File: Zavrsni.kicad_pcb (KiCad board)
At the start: 2 copper layers, 139.7 x 81.3 mm, 7 parts, among them J1 JOYSTICK, J2 LSM6DS3, J3 ILI9341, J4 NUCLEO-H743ZI2, J5 NUCLEO-H743ZI2, J6 NUCLEO-H743ZI2, J7 NUCLEO-H743ZI2

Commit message: Add files via upload
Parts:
- added C1: 100 nF, Capacitor_SMD:C_0603_1608Metric, F.Cu at (47.9, 36.7)
- added C2: C, Capacitor_SMD:C_0603_1608Metric, F.Cu at (47.9, 39.2)
- added C3: C, Capacitor_SMD:C_0603_1608Metric, F.Cu at (47.9, 41.7)
- added C4: C, Capacitor_SMD:C_0603_1608Metric, F.Cu at (47.9, 44.2)
- added C5: C, Capacitor_SMD:C_0603_1608Metric, F.Cu at (47.9, 46.8)
- added R1: 10k, Resistor_SMD:R_0201_0603Metric, F.Cu at (51.1, 36.3)
- added R2: 10k, Resistor_SMD:R_0201_0603Metric, F.Cu at (51.1, 38.1)
- added R3: 10k, Resistor_SMD:R_0201_0603Metric, F.Cu at (51.1, 39.8)
- added R4: 10k, Resistor_SMD:R_0201_0603Metric, F.Cu at (51.1, 41.6)
- added R5: 10k, Resistor_SMD:R_0201_0603Metric, F.Cu at (51.1, 43.3)
- added R6: 10k, Resistor_SMD:R_0201_0603Metric, F.Cu at (51.1, 45.1)
- moved J7 90.0 mm to (106.0, 107.3)
- moved J5 19.0 mm to (154.3, 102.6), turned to 0 degrees
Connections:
- J3 pad 3: /CS -> Net-(J3-Pin_3)
- J3 pad 6: /SDI -> Net-(J3-Pin_6)
- J3 pad 7: /SCK -> Net-(J3-Pin_7)
- J3 pad 9: /SDO(MISO) -> Net-(J3-Pin_9)
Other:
- board size 139.7 x 81.3 mm -> 70 x 135 mm

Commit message: Add files via upload
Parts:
- added C6: 10nF, Capacitor_SMD:C_0603_1608Metric, F.Cu at (63.9, 108.3)
- added C7: 4,7uF, Capacitor_SMD:C_0603_1608Metric, F.Cu at (63.9, 110.8)
- added C8: 4,7uF, Capacitor_SMD:C_0603_1608Metric, F.Cu at (63.9, 113.3)
- added J8: Conn_02x35_Odd_Even, Connector_PinHeader_2.54mm:PinHeader_2x35_P2.54mm_Vertical, F.Cu at (248.3, 56.5)
- added J9: Conn_02x35_Odd_Even, Connector_PinHeader_2.54mm:PinHeader_2x35_P2.54mm_Vertical, F.Cu at (193.8, 56.5)
- added K1: JST-2pin-SMD, JST conector:jst connector, F.Cu at (63.6, 83.6)
- added R7: 10k, Resistor_SMD:R_0603_1608Metric, F.Cu at (63.9, 115.8)
- added SW1: SW_Push, Button_Switch_SMD:SW_Push_1P1T_NO_6x6mm_H9.5mm, F.Cu at (56.4, 110.8)
- added SW2: SW_Push, Button_Switch_SMD:SW_Push_1P1T_NO_6x6mm_H9.5mm, F.Cu at (56.4, 118.4)
- C2, C3, C4, C5: value C -> 100nF
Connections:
- net GND renamed Earth
- J5 pad 1: unconnected-(J5-Pin_1-Pad1) -> /D7
- J5 pad 4: unconnected-(J5-Pin_4-Pad4) -> /D4
- R5 pad 2: unconnected-(R5-Pad2) -> /D7
- R6 pad 1: unconnected-(R6-Pad1) -> +3.3V
- R6 pad 2: unconnected-(R6-Pad2) -> /D4
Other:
- board size 70 x 135 mm -> 151.2 x 133.3 mm

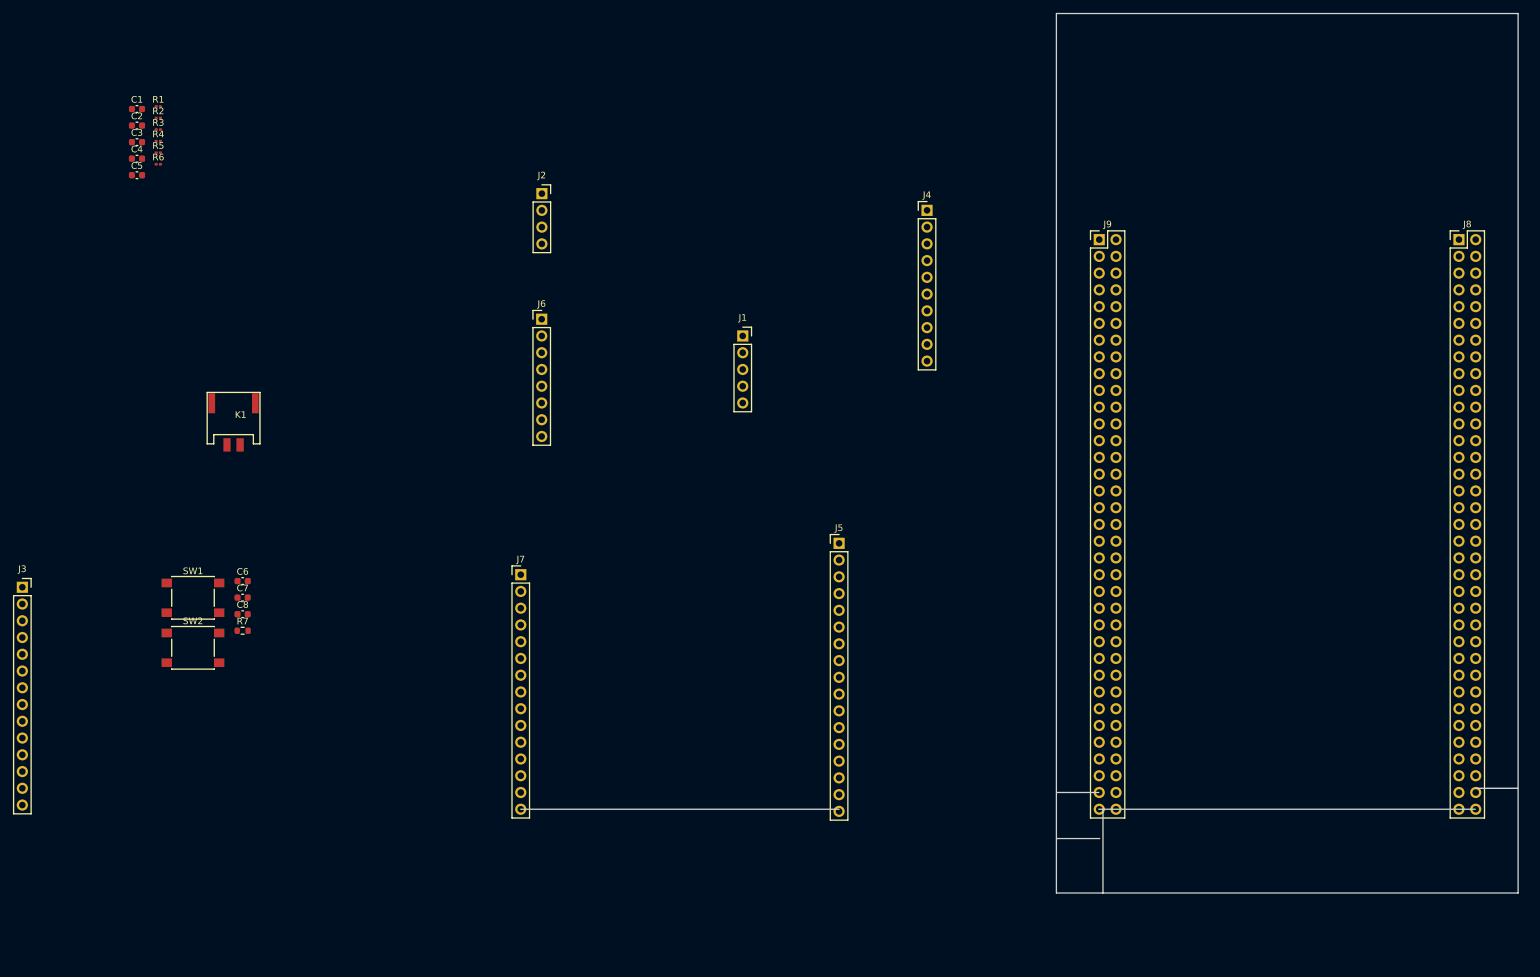
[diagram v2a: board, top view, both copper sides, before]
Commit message: Start connecting the lines on the pcb
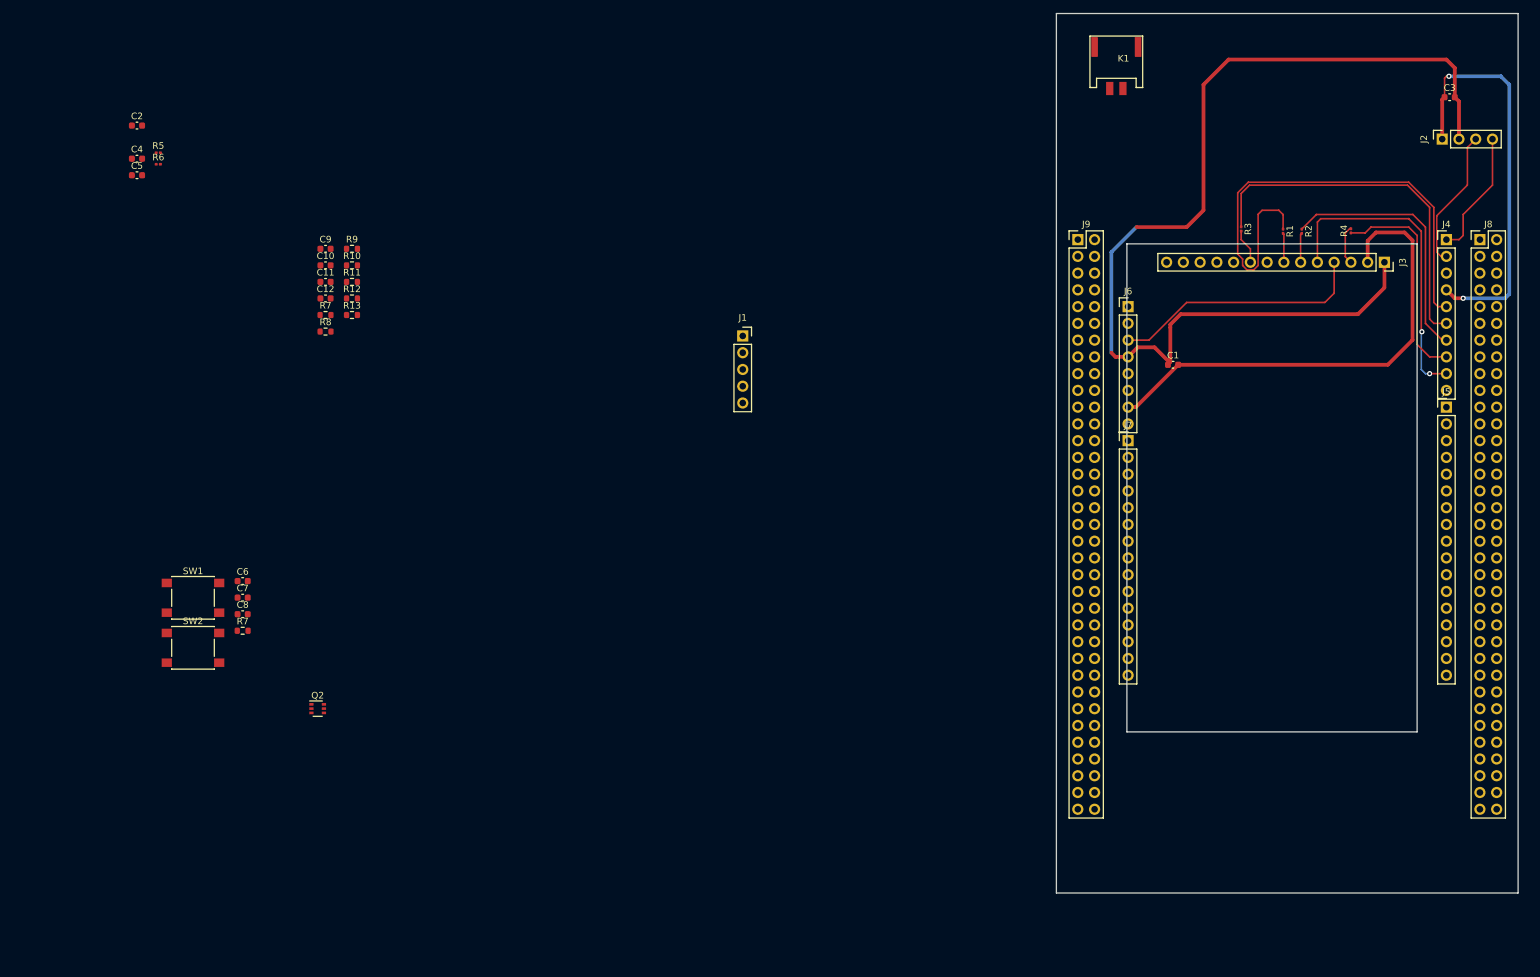
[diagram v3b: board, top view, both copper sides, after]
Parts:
- added C10: 10nF, Capacitor_SMD:C_0603_1608Metric, F.Cu at (76.4, 60.4)
- added C11: 10nF, Capacitor_SMD:C_0603_1608Metric, F.Cu at (76.4, 62.9)
- added C12: 10uF, Capacitor_SMD:C_0603_1608Metric, F.Cu at (76.4, 65.4)
- added C9: 10nF, Capacitor_SMD:C_0603_1608Metric, F.Cu at (76.4, 57.9)
- added Q2: BSD235C, Package_TO_SOT_SMD:SOT-363_SC-70-6, F.Cu at (75.2, 127.6)
- added R10: 100R, Resistor_SMD:R_0603_1608Metric, F.Cu at (80.5, 60.4)
- added R11: 10k, Resistor_SMD:R_0603_1608Metric, F.Cu at (80.5, 62.9)
- added R12: 100R, Resistor_SMD:R_0603_1608Metric, F.Cu at (80.5, 65.4)
- added R13: 100R, Resistor_SMD:R_0603_1608Metric, F.Cu at (80.5, 67.9)
- added R7: 1k, Resistor_SMD:R_0603_1608Metric, F.Cu at (76.4, 67.9)
- added R8: 100R, Resistor_SMD:R_0603_1608Metric, F.Cu at (76.4, 70.5)
- added R9: 100R, Resistor_SMD:R_0603_1608Metric, F.Cu at (80.5, 57.9)
- C6: value 10nF -> 10uF
- C7, C8: value 4,7uF -> 10nF
- R1, R2, R3, R4: value 10k -> 330R
- moved J3 212.3 mm to (237.0, 59.9), turned to -90 degrees
- moved C3 199.1 mm to (246.9, 34.9)
- moved R4 181.3 mm to (231.9, 55.2), turned to 90 degrees
- moved R2 174.2 mm to (224.4, 55.2), turned to -90 degrees
- moved R1 171.6 mm to (221.6, 55.2), turned to -90 degrees
- moved R3 164.9 mm to (215.3, 54.9), turned to -90 degrees
- moved C1 161.8 mm to (204.9, 75.5)
- moved K1 144.3 mm to (197.4, 29.6)
- moved J2 136.7 mm to (245.7, 41.3), turned to 90 degrees
- moved J5 94.4 mm to (246.4, 81.9)
- moved J7 94.3 mm to (198.1, 87.0)
- moved J6 88.9 mm to (198.1, 66.7)
- moved J4 78.9 mm to (246.4, 56.5)
- moved J9 3.25 mm to (190.5, 56.5)
- moved J8 3.18 mm to (251.5, 56.5)
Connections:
- net /VBAT renamed VCC
- net Net-(J3-Pin_9) renamed /SDO
- J1 pad 3: /VRx -> Net-(J1-Pin_3)
- J1 pad 4: /VRy -> Net-(J1-Pin_4)
- J1 pad 5: /SW -> Net-(J1-Pin_5)
- J3 pad 3: Net-(J3-Pin_3) -> /CS
- J3 pad 6: Net-(J3-Pin_6) -> /SDI
- J3 pad 7: Net-(J3-Pin_7) -> /SCK
- J4 pad 1: unconnected-(J4-Pin_1-Pad1) -> /SCL
- J4 pad 10: /ŞW -> /SW
- J4 pad 2: unconnected-(J4-Pin_2-Pad2) -> /SDA
- J4 pad 5: /SCK -> /SCK(D13)
- J4 pad 6: /MISO -> /SDO(MISO)
- J4 pad 7: /MOSI -> /SDI(MOSI)
- J4 pad 8: /CS -> /CSN
- J4 pad 9: /LED -> /DC/RS
- J5 pad 2: unconnected-(J5-Pin_2-Pad2) -> /LED
- R1 pad 1: /SCK -> /SCK(D13)
- R1 pad 2: Net-(J3-Pin_7) -> /SCK
- R2 pad 1: /SDI -> /SDI(MOSI)
- R2 pad 2: Net-(J3-Pin_6) -> /SDI
- R4 pad 1: /CS -> /CSN
- R4 pad 2: Net-(J3-Pin_3) -> /CS
- SW1 pad 2: /D4 -> Net-(R13-Pad1)
- SW2 pad 2: /D7 -> Net-(R12-Pad1)
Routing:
- net +3V3: track 0.00 -> 157.5 mm
- net Earth: track 0.00 -> 136.0 mm, vias 0 -> 2
- net /SCK(D13): track 0.00 -> 77.1 mm
- net /SDO(MISO): track 0.00 -> 55.3 mm
- net /DC/RS: track 0.00 -> 48.0 mm, vias 0 -> 2
- net /SDI(MOSI): track 0.00 -> 39.3 mm
- net /RST: track 0.00 -> 38.9 mm
- net /CSN: track 0.00 -> 32.7 mm
- net /SDA: track 0.00 -> 21.3 mm
- net /SCL: track 0.00 -> 19.2 mm
- net /CS: track 0.00 -> 5.90 mm
- net /SDO: track 0.00 -> 5.30 mm
- net /SDI: track 0.00 -> 4.45 mm
- net /SCK: track 0.00 -> 4.43 mm
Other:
- board size 151.2 x 133.3 mm -> 70 x 133.3 mm

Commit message: Add files via upload
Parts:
- removed J1: JOYSTICK, Connector_PinSocket_2.54mm:PinSocket_1x05_P2.54mm_Vertical
- removed J2: LSM6DS3, Connector_PinSocket_2.54mm:PinSocket_1x04_P2.54mm_Vertical
- removed J3: ILI9341, Connector_PinSocket_2.54mm:PinSocket_1x14_P2.54mm_Vertical
- removed J4: NUCLEO-H743ZI2, Connector_PinHeader_2.54mm:PinHeader_1x10_P2.54mm_Vertical
- removed J5: NUCLEO-H743ZI2, Connector_PinHeader_2.54mm:PinHeader_1x17_P2.54mm_Vertical
- removed J6: NUCLEO-H743ZI2, Connector_PinHeader_2.54mm:PinHeader_1x08_P2.54mm_Vertical
- removed J7: NUCLEO-H743ZI2, Connector_PinHeader_2.54mm:PinHeader_1x15_P2.54mm_Vertical
- removed J8, J9: Conn_02x35_Odd_Even, Connector_PinHeader_2.54mm:PinHeader_2x35_P2.54mm_Vertical
- removed Q2: BSD235C, Package_TO_SOT_SMD:SOT-363_SC-70-6
- removed R7: 1k, Resistor_SMD:R_0603_1608Metric
- removed R7: 10k, Resistor_SMD:R_0603_1608Metric
- added DISP1: LCD TFT ILI9341, BornaKiCad:LCD_TFT_2.4, F.Cu at (222.2, 105.6)
- added JOYSTICK_HW_1: ~, JOYSTICK:JOYSTICK, F.Cu at (229.2, 43.8)
- added LSM6DS1: ~, LSMDS3_akceleometar_žiroskop:LSM6DS3, F.Cu at (197.6, 44.5)
- added NMOS2: ~, Package_TO_SOT_SMD:SOT-23-3, F.Cu at (238.0, 148.9)
- added NUCLEO_144_H743ZI2: ~, NUCLEO_PCB:NUCLEO_PCB, F.Cu at (223.5, 92.6)
- added PMOS1: ~, Package_TO_SOT_SMD:SOT-23-3, F.Cu at (226.7, 147.8)
- added R14: 4,7k, Resistor_SMD:R_0603_1608Metric, F.Cu at (208.9, 41.1)
- added R15: 4,7k, Resistor_SMD:R_0603_1608Metric, F.Cu at (208.9, 32.8)
- added R16: 10k, Resistor_SMD:R_0603_1608Metric, F.Cu at (231.1, 147.1)
- added R17: 10k, Resistor_SMD:R_0603_1608Metric, F.Cu at (148.4, 165.7)
- R1, R2, R3, R4: footprint Resistor_SMD:R_0201_0603Metric -> Resistor_SMD:R_0603_1608Metric
- R5, R6: footprint Resistor_SMD:R_0201_0603Metric -> Capacitor_SMD:C_0603_1608Metric
- moved C4 160.4 mm to (208.3, 47.1), turned to -90 degrees
- moved C3 155.8 mm to (144.6, 152.5)
- moved R6 149.6 mm to (152.6, 155.0)
- moved R5 149.1 mm to (152.6, 152.5)
- moved C2 147.0 mm to (144.6, 149.9)
- moved C5 147.0 mm to (144.6, 157.5)
- moved R10 125.0 mm to (152.6, 162.5)
- moved R9 125.0 mm to (152.6, 160.0)
- moved C10 117.0 mm to (148.6, 152.5)
- moved C11 117.0 mm to (148.6, 155.0)
- moved C12 117.0 mm to (148.6, 157.5)
- moved C9 117.0 mm to (148.6, 149.9)
- moved R8 115.7 mm to (152.6, 157.5)
- moved R13 113.8 mm to (156.7, 152.5)
- moved R11 113.8 mm to (156.7, 147.4)
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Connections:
- C1 pad 1: +3V3 -> +3.3V
- C12 pad 2: VCC -> +3.3V
- C2 pad 2: +3V3 -> +3.3V
- C3 pad 2: +3V3 -> +3.3V
- C4 pad 1: +3V3 -> +3.3V
- C5 pad 1: +3V3 -> +3.3V
- C6 pad 2: VCC -> +3.3V
- K1 pad 1: VCC -> +3.3V
- R1 pad 1: /SCK(D13) -> /SCK
- R1 pad 2: /SCK -> /SCK(D13)
- R10 pad 1: Net-(J1-Pin_5) -> /SW
- R10 pad 2: /SW -> Net-(JOYSTICK_HW_1-SW)
- R11 pad 1: VCC -> /SW
- R11 pad 2: /SW -> +3.3V
- R2 pad 1: /SDI(MOSI) -> /SDI
- R2 pad 2: /SDI -> /SDI(MOSI)
- R5 pad 1: unconnected-(R5-Pad1) -> +3.3V
- R8 pad 1: /VRx -> Net-(JOYSTICK_HW_1-VRx)
- R8 pad 2: Net-(J1-Pin_3) -> /VRx
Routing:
- net +3.3V: track 0.00 -> 369.2 mm, vias 0 -> 6
- net +3V3: track 157.5 -> 0.00 mm
- net /NRST: track 0.00 -> 107.2 mm, vias 0 -> 2
- net /CSN: track 32.7 -> 122.7 mm
- net /SDI(MOSI): track 39.3 -> 112.9 mm, vias 0 -> 1
- net /DC/RS: track 48.0 -> 118.7 mm, vias 2 -> 1
- net /SCL: track 19.2 -> 68.8 mm
- net /SDA: track 21.3 -> 61.4 mm, vias 0 -> 2
- net /RST: track 38.9 -> 0.00 mm
- net /SCK(D13): track 77.1 -> 112.7 mm, vias 0 -> 2
- net /SDO(MISO): track 55.3 -> 79.8 mm, vias 0 -> 2
- net Earth: track 136.0 -> 157.8 mm, vias 2 -> 3
- net /D: track 0.00 -> 20.9 mm
- net /SDO: track 5.30 -> 21.3 mm
- net Net-(LSM6DS1-SCL): track 0.00 -> 11.0 mm
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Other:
- board outline removed

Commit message: Add files via upload
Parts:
- moved R10 157.2 mm to (244.5, 34.9), turned to 180 degrees
- moved C11 156.4 mm to (248.9, 34.9)
- moved R9 148.8 mm to (243.2, 41.9), turned to 180 degrees
- moved C10 148.7 mm to (244.5, 38.7)
- moved R11 148.6 mm to (249.1, 31.1)
- moved R8 146.8 mm to (247.0, 45.1)
- moved C9 146.1 mm to (247.0, 41.9), turned to 180 degrees
- moved C2 140.3 mm to (243.2, 50.2), turned to 180 degrees
- moved LSM6DS1 72.0 mm to (223.0, 111.8), turned to 90 degrees
- moved R14 69.5 mm to (151.8, 80.6)
- moved C4 37.4 mm to (172.7, 35.7)
- moved R15 37.1 mm to (173.1, 42.6)
- moved JOYSTICK_HW_1 6.09 mm to (223.3, 45.2)
- moved R1 2.77 mm to (220.8, 147.1)
- moved C1 1.97 mm to (205.8, 146.4)
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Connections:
- net Net-(JOYSTICK_HW_1-SW) renamed /T1
- net Net-(JOYSTICK_HW_1-VRx) renamed /dirX
- net Net-(JOYSTICK_HW_1-VRy) renamed /dirY
- NUCLEO_144_H743ZI2 pad 17: /A0 -> /VRx
- NUCLEO_144_H743ZI2 pad 19: /A1 -> /VRy
- NUCLEO_144_H743ZI2 pad 48: /SCL -> +3.3V
- NUCLEO_144_H743ZI2 pad 50: /SDA -> +3.3V
- R14 pad 1: /SDA -> +3.3V
- R15 pad 1: /SCL -> +3.3V
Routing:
- net Earth: track 157.8 -> 10.3 mm, vias 3 -> 0
- net /VRy: track 0.00 -> 111.1 mm, vias 0 -> 4
- net /VRx: track 0.00 -> 97.7 mm, vias 0 -> 3
- net /SW: track 0.00 -> 85.9 mm, vias 0 -> 2
- net /SCL: track 68.8 -> 0.00 mm
- net /LED(PWM): track 0.00 -> 65.8 mm, vias 0 -> 2
- net /SDA: track 61.4 -> 0.00 mm, vias 2 -> 0
- net +3.3V: track 369.2 -> 346.1 mm, vias 6 -> 3
- net Net-(LSM6DS1-SCL): track 11.0 -> 0.00 mm
- net /dirX: track 0.00 -> 7.64 mm
- net /T1: track 0.00 -> 7.29 mm
- net Net-(LSM6DS1-SDA): track 5.65 -> 0.00 mm
- net /NRST: track 107.2 -> 112.7 mm, vias 2 -> 4
- net /dirY: track 0.00 -> 4.09 mm
- net /SCK: track 6.50 -> 3.76 mm
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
